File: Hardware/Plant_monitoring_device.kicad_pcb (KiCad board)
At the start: 2 copper layers, 88 x 58 mm, 70 parts, among them J1 Barrel_Jack, J10 LED_PWM4, J11 SOIL1, J12 SOIL2, J13 SOIL3, J14 SOIL4, J2 SWO, J3 OUT1, J4 OUT2, J5 OUT3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

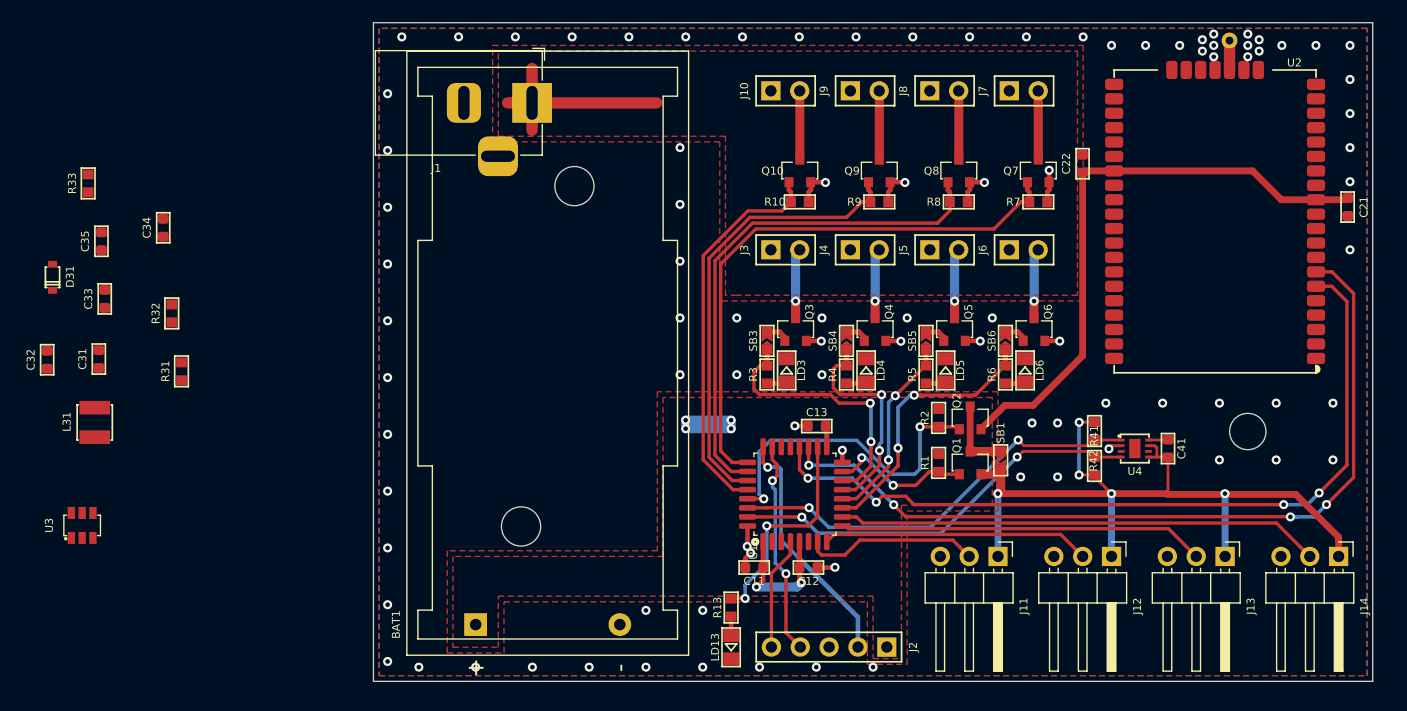
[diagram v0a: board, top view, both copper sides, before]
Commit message: Changes Step-down for LDO.
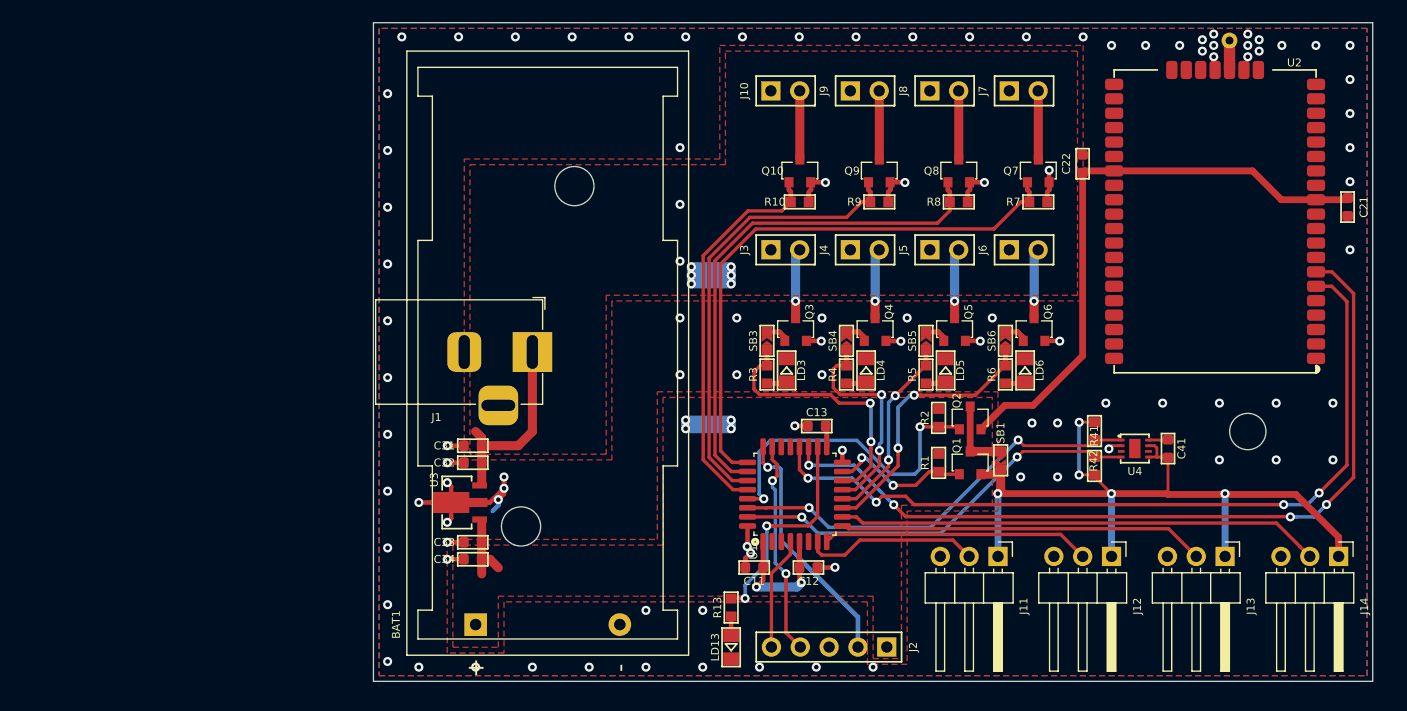
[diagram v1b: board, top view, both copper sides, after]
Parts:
- removed C35: 1uF, MRS_Passives:C0603
- removed D31: CUS10F30, MRS_Diodes:SOD-323
- removed L31: 4u7, MRS_Passives:L_DJNR3015
- removed R31, R33: 10k, MRS_Passives:R0603
- removed R32: 140k, MRS_Passives:R0603
- C33: value 0.1uF -> 10uF
- C34: value 10uF -> 1uF
- U3: value AOZ1282CI-1 -> AP2204RB-3.3TRG1; footprint MRS_SOT:SOT-23-6 -> MRS_SOT:SOT-89
- moved C34 39.9 mm to (186.8, 141.2), turned to 180 degrees
- moved C33 38.9 mm to (186.8, 139.8), turned to 180 degrees
- moved C32 38.6 mm to (186.8, 132.8), turned to 180 degrees
- moved C31 33.8 mm to (186.8, 131.2), turned to 180 degrees
- moved U3 33.1 mm to (185.3, 136.2)
- moved J1 21.9 mm to (192.0, 123.0)
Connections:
- C33 pad 1: Net-(C33-Pad1) -> VCC
- C33 pad 2: Net-(C33-Pad2) -> GND
- U3 pad 1: Net-(C33-Pad1) -> VCC
- U3 pad 3: Net-(R32-Pad2) -> +12V
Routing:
- net GND: track 27.3 -> 45.5 mm, vias 93 -> 103
- net +12V: track 18.6 -> 30.2 mm, vias 0 -> 6
- net VCC: track 30.1 -> 36.4 mm

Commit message: Changes 2.54mm headers for 2mm connectors. Added a solderbridge to connect external supply with the mcu suply (so the outpust and pwms coul be used when the device is powered by a battery. Changed layout of the connectors. Made the PCB smaller.
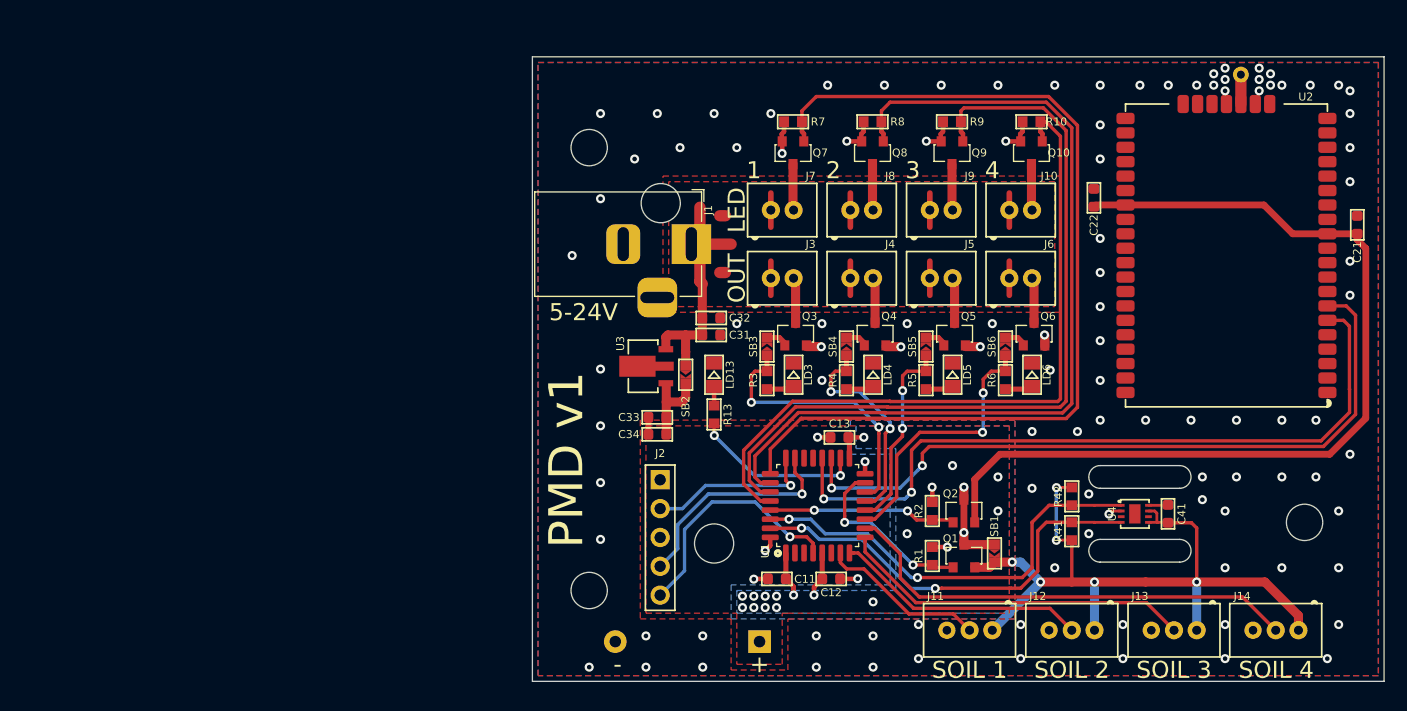
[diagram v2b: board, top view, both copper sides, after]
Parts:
- added H2: Mounting_hole_unplated_3,2mm, MRS_Mechanical:Mounting_hole_unplated_3,2mm, F.Cu at (197.0, 144.0)
- added H3: Mounting_hole_unplated_3,2mm, MRS_Mechanical:Mounting_hole_unplated_3,2mm, F.Cu at (197.0, 105.0)
- added SB2: SolderBridge, MRS_Connectors:SB0603, F.Cu at (205.5, 125.0)
- BAT1: moved to B.Cu
- J10: value LED_PWM4 -> NXW-02; footprint MRS_Connectors:Header_1x02_P2.54mm -> MRS_Connectors:NXW-02
- J11: value SOIL1 -> NXW-03; footprint MRS_Connectors:Header_1x03_P2.54mm_Horizontal -> MRS_Connectors:NXW-03
- J12: value SOIL2 -> NXW-03; footprint MRS_Connectors:Header_1x03_P2.54mm_Horizontal -> MRS_Connectors:NXW-03
- J13: value SOIL3 -> NXW-03; footprint MRS_Connectors:Header_1x03_P2.54mm_Horizontal -> MRS_Connectors:NXW-03
- J14: value SOIL4 -> NXW-03; footprint MRS_Connectors:Header_1x03_P2.54mm_Horizontal -> MRS_Connectors:NXW-03
- J3: value OUT1 -> NXW-02; footprint MRS_Connectors:Header_1x02_P2.54mm -> MRS_Connectors:NXW-02
- J4: value OUT2 -> NXW-02; footprint MRS_Connectors:Header_1x02_P2.54mm -> MRS_Connectors:NXW-02
- J5: value OUT3 -> NXW-02; footprint MRS_Connectors:Header_1x02_P2.54mm -> MRS_Connectors:NXW-02
- J6: value OUT4 -> NXW-02; footprint MRS_Connectors:Header_1x02_P2.54mm -> MRS_Connectors:NXW-02
- J7: value LED_PWM1 -> NXW-02; footprint MRS_Connectors:Header_1x02_P2.54mm -> MRS_Connectors:NXW-02
- J8: value LED_PWM2 -> NXW-02; footprint MRS_Connectors:Header_1x02_P2.54mm -> MRS_Connectors:NXW-02
- J9: value LED_PWM3 -> NXW-02; footprint MRS_Connectors:Header_1x02_P2.54mm -> MRS_Connectors:NXW-02
- moved BAT1 25.0 mm to (212.0, 148.5)
- moved J2 24.8 mm to (203.2, 134.2), turned to 0 degrees
- moved C32 24.6 mm to (207.8, 120.0), turned to 0 degrees
- moved LD13 24.0 mm to (208.0, 125.0), turned to 270 degrees
- moved J10 23.5 mm to (234.0, 110.5), turned to 0 degrees
- moved J7 23.5 mm to (213.0, 110.5), turned to 0 degrees
- moved C31 23.2 mm to (207.8, 121.5), turned to 0 degrees
- moved R7 22.7 mm to (214.9, 102.7), turned to 180 degrees
- moved Q7 21.7 mm to (214.9, 105.5), turned to 270 degrees
- moved R10 21.6 mm to (235.9, 102.7), turned to 180 degrees
- moved Q10 20.5 mm to (235.9, 105.5), turned to 270 degrees
- moved U3 20.3 mm to (201.8, 124.2)
- moved C33 19.6 mm to (203.0, 128.8)
- moved C34 19.6 mm to (203.0, 130.2)
- moved R13 17.1 mm to (208.0, 128.5), turned to 90 degrees
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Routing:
- net /LED_PWM1: track 50.5 -> 84.7 mm
- net /LED_PWM2: track 45.7 -> 78.8 mm
- net /LED_PWM3: track 39.8 -> 71.8 mm
- net VDD: track 52.3 -> 81.1 mm
- net /LED_PWM4: track 34.5 -> 63.0 mm
- net +12V: track 30.2 -> 48.7 mm, vias 6 -> 0
- net GND: track 45.5 -> 27.8 mm, vias 103 -> 110
- net /COMM_ENA: track 29.0 -> 16.6 mm
- net /NRST: track 9.98 -> 21.4 mm, vias 0 -> 1
- net /UART_TX: track 73.2 -> 63.7 mm, vias 4 -> 2
- net VCC: track 36.4 -> 29.0 mm, vias 6 -> 20
- net /SWCLK: track 21.7 -> 14.9 mm
- net /UART_RX: track 71.1 -> 65.0 mm, vias 4 -> 2
- net /BAT_LO: track 19.4 -> 15.2 mm
- net /SENS_ENA: track 12.3 -> 15.6 mm
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- added copper zone on B.Cu, net VCC
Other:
- board size 88 x 58 mm -> 75 x 55 mm
- board text added: "+"
- board text added: "-"
- board text added: "1"
- board text added: "2"
- board text added: "3"
- board text added: "4"
- board text added: "5-24V"
- board text added: "LED"
- board text added: "OUT"
- board text added: "PMD v1"
- board text added: "SOIL 1"
- board text added: "SOIL 2"
- board text added: "SOIL 3"
- board text added: "SOIL 4"

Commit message: Swapped some pins to optmize track to tranzistors. Generated Gerbers.
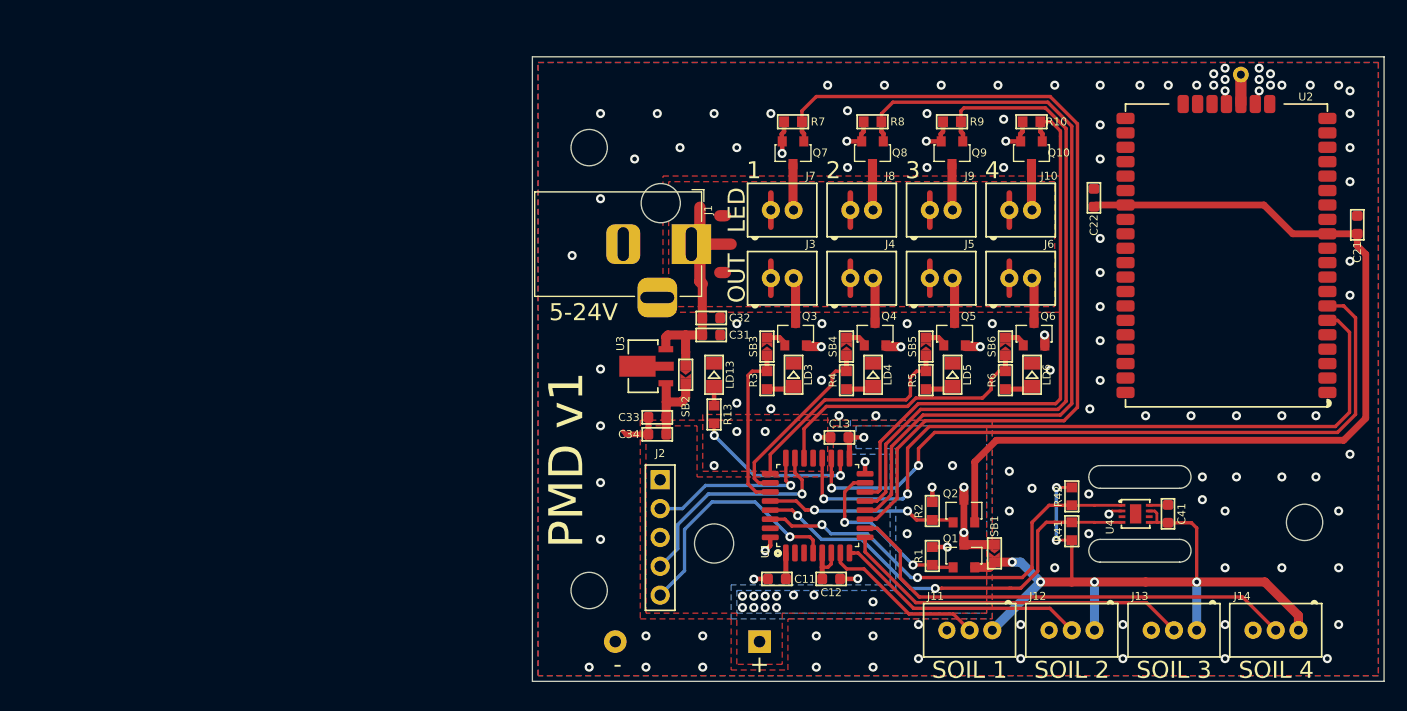
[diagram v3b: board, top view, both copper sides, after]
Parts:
- R13, R3, R4, R5, R6: value R -> 1k
- moved U4 0.07 mm to (245.1, 137.2)
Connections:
- net /ADC_PH1 renamed /ADC_SOIL1
- net /ADC_PH2 renamed /ADC_SOIL2
- net /ADC_PH3 renamed /ADC_SOIL3
- net /ADC_PH4 renamed /ADC_SOIL4
- net /USB_D- renamed /PA11
- U1 pad 11: /OUT4 -> /LED_PWM1
- U1 pad 12: /OUT3 -> /LED_PWM2
- U1 pad 13: /OUT2 -> /LED_PWM3
- U1 pad 14: /OUT1 -> /LED_PWM4
- U1 pad 22: /USB_D+ -> /OUT4
- U1 pad 25: /LED_PWM1 -> /OUT3
- U1 pad 26: /LED_PWM2 -> /OUT2
- U1 pad 27: /LED_PWM3 -> /OUT1
- U1 pad 28: /LED_PWM4 -> /COMM_ENA
- U1 pad 29: /COMM_ENA -> /I2C_SCL
- U1 pad 31: /I2C_SCL -> Net-(U1-Pad31)
- U1 pad 6: /ADC_BAT -> VCC
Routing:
- net /LED_PWM4: track 63.0 -> 50.6 mm
- net /LED_PWM3: track 71.8 -> 61.2 mm
- net /OUT1: track 24.2 -> 15.0 mm, vias 2 -> 0
- net /LED_PWM2: track 78.8 -> 70.0 mm
- net /LED_PWM1: track 84.7 -> 79.3 mm
- net /OUT3: track 17.3 -> 20.8 mm, vias 2 -> 0
- net /OUT2: track 19.0 -> 16.3 mm, vias 2 -> 0
- net GND: track 27.8 -> 30.1 mm, vias 110 -> 123
- net VCC: track 29.0 -> 27.4 mm, vias 20 -> 18
- net VDD: track 81.1 -> 82.0 mm
- net /I2C_SCL: track 37.7 -> 38.3 mm
- net /OUT4: track 24.0 -> 24.3 mm, vias 2 -> 0

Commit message: Added dimensions.
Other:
- board text added: "ANT"

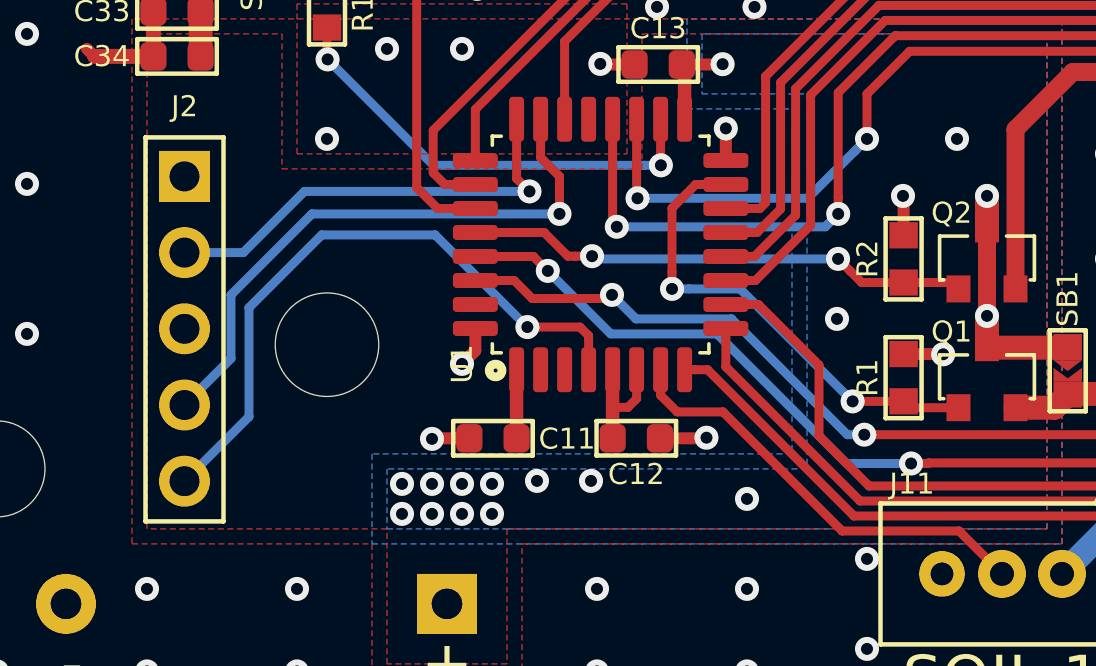
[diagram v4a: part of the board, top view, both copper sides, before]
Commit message: Connected BOOT0 pin with GND.
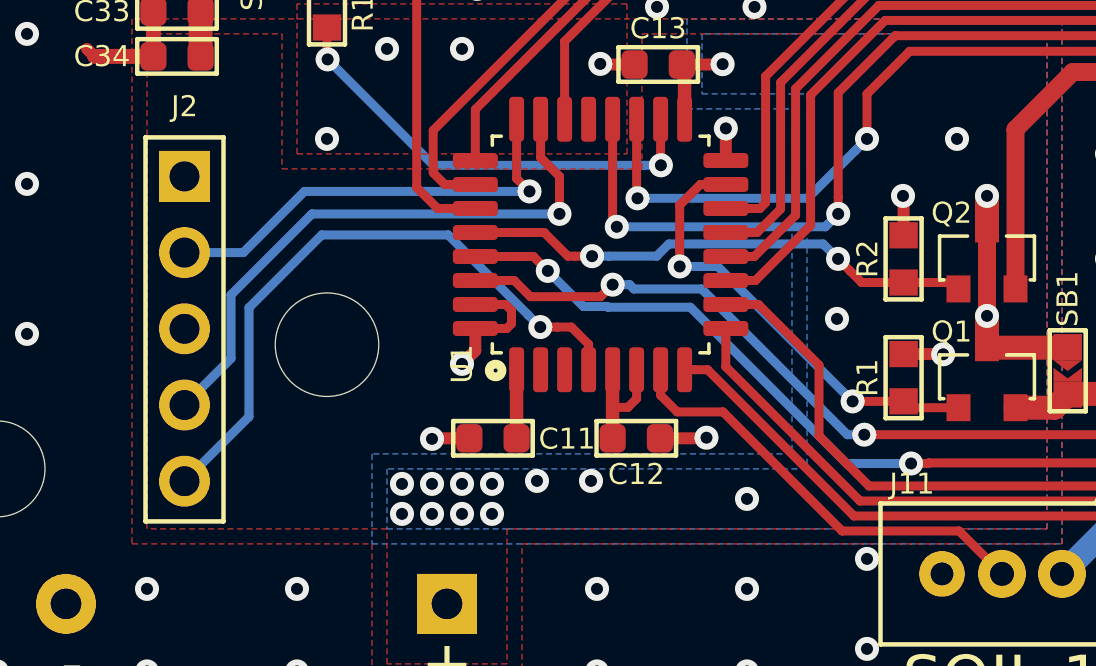
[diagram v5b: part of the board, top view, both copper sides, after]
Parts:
- LD13: value ORANGE -> RED
- LD3, LD4, LD5, LD6: value RED -> ORANGE
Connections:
- U1 pad 31: Net-(U1-Pad31) -> GND
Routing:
- net GND: track 30.1 -> 33.1 mm
- net /SENS_ENA: track 15.7 -> 14.8 mm
